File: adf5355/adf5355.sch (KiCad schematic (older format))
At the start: 96 parts, among them J1 REF_IN_A, J2 RF_B, J3 RF_A_P, J4 REF_IN_B, J5 RF_A_N, J6 Conn_01x02_Male, J7 Conn_01x10_Male, U1 L7806, U2 ADM7150, U3 ADM7150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

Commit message: Layout fully routed, now needs finilizing, moving vias to make better powerplanes, route diffpairs properly etc.
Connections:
- net labels added: GNDA
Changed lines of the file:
@@
 	6150 4900 6050 4900
 Wire Wire Line
-	5550 4900 5550 4800
-Wire Wire Line
 	5650 4800 5650 4900
-Connection ~ 5650 4900
-Wire Wire Line
-	5650 4900 5550 4900
 Wire Wire Line
 	5750 4800 5750 4900
@@
 Wire Wire Line
 	1800 6650 2100 6650
-Wire Wire Line
-	1800 6750 2100 6750
 Wire Wire Line
 	1800 6950 2100 6950
@@
 Text Label 1950 6650 0    50   ~ 0
 DATA
+Text Label 1950 6850 0    50   ~ 0
+LE
 Text Label 1950 6750 0    50   ~ 0
-LE
-Text Label 1950 6850 0    50   ~ 0
 MUX
 Wire Wire Line
@@
 	0    1    1    0
 $EndComp
-$Comp
-L power:GND #PWR053
-U 1 1 5BFF4BA3
-P 7500 5050
-F 0 "#PWR053" H 7500 4800 50  0001 C CNN
-F 1 "GND" H 7505 4877 50  0000 C CNN
-F 2 "" H 7500 5050 50  0001 C CNN
-F 3 "" H 7500 5050 50  0001 C CNN
-	1    7500 5050
-	1    0    0    -1
-$EndComp
-$Comp
-L power:GND #PWR045
-U 1 1 5BFF4C62
-P 7850 4650
-F 0 "#PWR045" H 7850 4400 50  0001 C CNN
-F 1 "GND" H 7855 4477 50  0000 C CNN
-F 2 "" H 7850 4650 50  0001 C CNN
-F 3 "" H 7850 4650 50  0001 C CNN
-	1    7850 4650
-	1    0    0    -1
-$EndComp
-$Comp
-L power:GND #PWR046
-U 1 1 5BFF4D21
-P 8400 4650
-F 0 "#PWR046" H 8400 4400 50  0001 C CNN
-F 1 "GND" H 8405 4477 50  0000 C CNN
-F 2 "" H 8400 4650 50  0001 C CNN
-F 3 "" H 8400 4650 50  0001 C CNN
-	1    8400 4650
-	1    0    0    -1
-$EndComp
-$Comp
-L power:GND #PWR047
-U 1 1 5BFF4DE0
-P 8900 4650
-F 0 "#PWR047" H 8900 4400 50  0001 C CNN
-F 1 "GND" H 8905 4477 50  0000 C CNN
-F 2 "" H 8900 4650 50  0001 C CNN
-F 3 "" H 8900 4650 50  0001 C CNN
-	1    8900 4650
-	1    0    0    -1
-$EndComp
 Wire Wire Line
 	7050 4300 7050 4050
@@
 	2500 7550 2500 7600
 Wire Wire Line
-	1800 6850 2500 6850
-Wire Wire Line
 	6950 3600 8300 3600
 Wire Wire Line
@@
 Wire Wire Line
 	2600 3450 2850 3450
+Wire Wire Line
+	2500 6850 2500 6750
+Wire Wire Line
+	1800 6750 2500 6750
+Wire Wire Line
+	1800 6850 2100 6850
+$Comp
+L power:GNDA #PWR?
+U 1 1 5C191443
+P 5550 5000
+F 0 "#PWR?" H 5550 4750 50  0001 C CNN
+F 1 "GNDA" H 5555 4827 50  0000 C CNN
+F 2 "" H 5550 5000 50  0001 C CNN
+F 3 "" H 5550 5000 50  0001 C CNN
+	1    5550 5000
+	1    0    0    -1
+$EndComp
+Wire Wire Line
+	5550 4800 5550 5000
+$Comp
+L power:GNDA #PWR?
+U 1 1 5C1A492E
+P 7500 5050
+F 0 "#PWR?" H 7500 4800 50  0001 C CNN
+F 1 "GNDA" H 7505 4877 50  0000 C CNN
+F 2 "" H 7500 5050 50  0001 C CNN
+F 3 "" H 7500 5050 50  0001 C CNN
+	1    7500 5050
+	1    0    0    -1
+$EndComp
+$Comp
+L power:GNDA #PWR?
+U 1 1 5C1A49F9
+P 7850 4650
+F 0 "#PWR?" H 7850 4400 50  0001 C CNN
+F 1 "GNDA" H 7855 4477 50  0000 C CNN
+F 2 "" H 7850 4650 50  0001 C CNN
+F 3 "" H 7850 4650 50  0001 C CNN
+	1    7850 4650
+	1    0    0    -1
+$EndComp
+$Comp
+L power:GNDA #PWR?
+U 1 1 5C1A4AC4
+P 8400 4650
+F 0 "#PWR?" H 8400 4400 50  0001 C CNN
+F 1 "GNDA" H 8405 4477 50  0000 C CNN
+F 2 "" H 8400 4650 50  0001 C CNN
+F 3 "" H 8400 4650 50  0001 C CNN
+	1    8400 4650
+	1    0    0    -1
+$EndComp
+$Comp
+L power:GNDA #PWR?
+U 1 1 5C1A4B8F
+P 8900 4650
+F 0 "#PWR?" H 8900 4400 50  0001 C CNN
+F 1 "GNDA" H 8905 4477 50  0000 C CNN
+F 2 "" H 8900 4650 50  0001 C CNN
+F 3 "" H 8900 4650 50  0001 C CNN
+	1    8900 4650
+	1    0    0    -1
+$EndComp
 $EndSCHEMATC

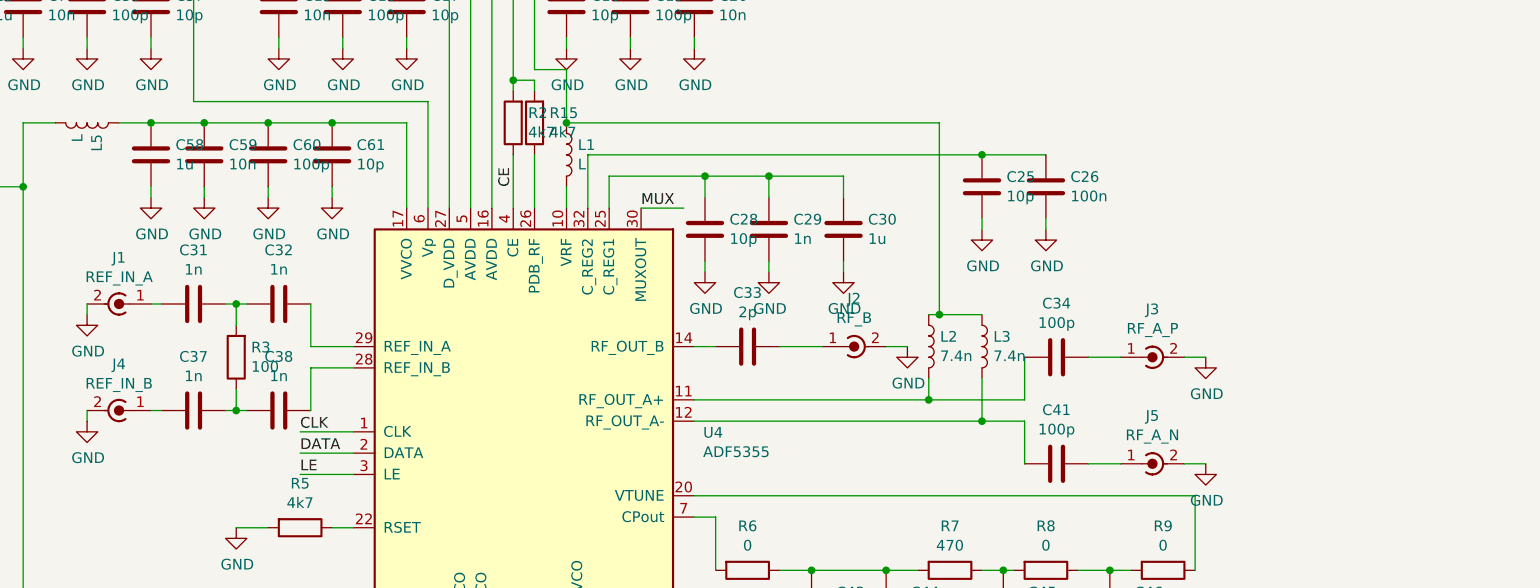
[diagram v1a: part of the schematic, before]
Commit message: Added some capacitors, better power planes etc. Needs fixing transmission lines and checking component placement for solderability. Also the c_reg capacitors probably needs to be closer to the pin
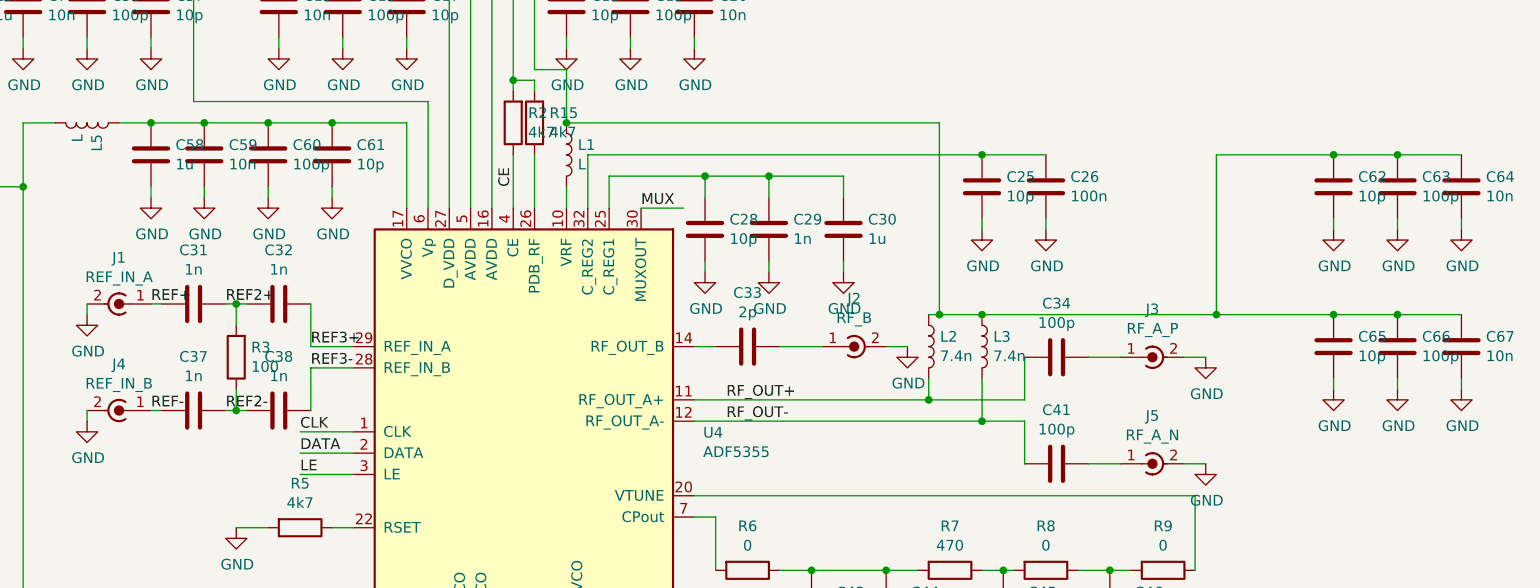
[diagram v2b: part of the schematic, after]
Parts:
- added C62, C65: 10p, Capacitors_SMD:C_0603, symbol Device:C
- added C63, C66: 100p, Capacitors_SMD:C_0603, symbol Device:C
- added C64, C67: 10n, Capacitors_SMD:C_0603, symbol Device:C
- C37: footprint Capacitors_SMD:C_0805 -> Capacitors_SMD:C_0603
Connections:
- net labels added: REF+, REF-, REF2+, REF2-, REF3+, REF3-, RF_OUT+, RF_OUT-
- wire segments 269 -> 283
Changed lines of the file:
@@
 F 0 "C37" V 4348 3550 50  0000 C CNN
 F 1 "1n" V 4439 3550 50  0000 C CNN
-F 2 "Capacitors_SMD:C_0805" H 4638 3400 50  0001 C CNN
+F 2 "Capacitors_SMD:C_0603" H 4638 3400 50  0001 C CNN
 F 3 "~" H 4600 3550 50  0001 C CNN
 	1    4600 3550
@@
 Connection ~ 3150 3250
 Wire Wire Line
-	6200 1500 6350 1500
-Wire Wire Line
 	6000 2600 6000 900
 Wire Wire Line
@@
 	1    0    0    -1
 $EndComp
-Connection ~ 6350 1500
-Wire Wire Line
-	6350 1500 6650 1500
 $Comp
 L Device:C C19
@@
 	1    0    0    -1
 $EndComp
-Connection ~ 6650 1500
-Wire Wire Line
-	6650 1500 6950 1500
 $Comp
 L Device:C C20
@@
 $EndComp
 Wire Wire Line
-	6950 1500 7300 1500
-Wire Wire Line
 	7300 1500 7300 1400
-Connection ~ 6950 1500
 Wire Wire Line
 	7300 1400 7300 900
@@
 Wire Wire Line
 	8300 3600 8500 3600
-Connection ~ 6350 2200
 $Comp
 L Device:R R15
@@
 	1800 6850 2100 6850
 $Comp
-L power:GNDA #PWR?
+L power:GNDA #PWR0109
 U 1 1 5C191443
 P 5550 5000
-F 0 "#PWR?" H 5550 4750 50  0001 C CNN
+F 0 "#PWR0109" H 5550 4750 50  0001 C CNN
 F 1 "GNDA" H 5555 4827 50  0000 C CNN
 F 2 "" H 5550 5000 50  0001 C CNN
@@
 	5550 4800 5550 5000
 $Comp
-L power:GNDA #PWR?
+L power:GNDA #PWR0110
 U 1 1 5C1A492E
 P 7500 5050
-F 0 "#PWR?" H 7500 4800 50  0001 C CNN
+F 0 "#PWR0110" H 7500 4800 50  0001 C CNN
 F 1 "GNDA" H 7505 4877 50  0000 C CNN
 F 2 "" H 7500 5050 50  0001 C CNN
@@
 $EndComp
 $Comp
-L power:GNDA #PWR?
+L power:GNDA #PWR0111
 U 1 1 5C1A49F9
 P 7850 4650
-F 0 "#PWR?" H 7850 4400 50  0001 C CNN
+F 0 "#PWR0111" H 7850 4400 50  0001 C CNN
 F 1 "GNDA" H 7855 4477 50  0000 C CNN
 F 2 "" H 7850 4650 50  0001 C CNN
@@
 $EndComp
 $Comp
-L power:GNDA #PWR?
+L power:GNDA #PWR0112
 U 1 1 5C1A4AC4
 P 8400 4650
-F 0 "#PWR?" H 8400 4400 50  0001 C CNN
+F 0 "#PWR0112" H 8400 4400 50  0001 C CNN
 F 1 "GNDA" H 8405 4477 50  0000 C CNN
 F 2 "" H 8400 4650 50  0001 C CNN
@@
 $EndComp
 $Comp
-L power:GNDA #PWR?
+L power:GNDA #PWR0113
 U 1 1 5C1A4B8F
 P 8900 4650
-F 0 "#PWR?" H 8900 4400 50  0001 C CNN
+F 0 "#PWR0113" H 8900 4400 50  0001 C CNN
 F 1 "GNDA" H 8905 4477 50  0000 C CNN
 F 2 "" H 8900 4650 50  0001 C CNN
@@
 	1    0    0    -1
 $EndComp
+Text Label 7100 3500 0    50   ~ 0
+RF_OUT+
+Text Label 7100 3600 0    50   ~ 0
+RF_OUT-
+Text Label 4400 3050 0    50   ~ 0
+REF+
+Text Label 4400 3550 0    50   ~ 0
+REF-
+Text Label 4750 3050 0    50   ~ 0
+REF2+
+Text Label 4750 3550 0    50   ~ 0
+REF2-
+Text Label 5150 3250 0    50   ~ 0
+REF3+
+Text Label 5150 3350 0    50   ~ 0
+REF3-
+Connection ~ 6350 2200
+Connection ~ 6950 1500
+Wire Wire Line
+	6950 1500 7300 1500
+Wire Wire Line
+	6650 1500 6950 1500
+Connection ~ 6650 1500
+Connection ~ 6350 1500
+Wire Wire Line
+	6350 1500 6650 1500
+Wire Wire Line
+	6200 1500 6350 1500
+$Comp
+L Device:C C62
+U 1 1 5C21E305
+P 9950 2500
+F 0 "C62" H 10065 2546 50  0000 L CNN
+F 1 "10p" H 10065 2455 50  0000 L CNN
+F 2 "Capacitors_SMD:C_0603" H 9988 2350 50  0001 C CNN
+F 3 "~" H 9950 2500 50  0001 C CNN
+	1    9950 2500
+	1    0    0    -1
+$EndComp
+$Comp
+L Device:C C63
+U 1 1 5C21E30B
+P 10250 2500
+F 0 "C63" H 10365 2546 50  0000 L CNN
+F 1 "100p" H 10365 2455 50  0000 L CNN
+F 2 "Capacitors_SMD:C_0603" H 10288 2350 50  0001 C CNN
+F 3 "~" H 10250 2500 50  0001 C CNN
+	1    10250 2500
+	1    0    0    -1
+$EndComp
+$Comp
+L Device:C C64
+U 1 1 5C21E311
+P 10550 2500
+F 0 "C64" H 10665 2546 50  0000 L CNN
+F 1 "10n" H 10665 2455 50  0000 L CNN
+F 2 "Capacitors_SMD:C_0603" H 10588 2350 50  0001 C CNN
+F 3 "~" H 10550 2500 50  0001 C CNN
+	1    10550 2500
+	1    0    0    -1
+$EndComp
+$Comp
+L power:GND #PWR0114
+U 1 1 5C21E317
+P 9950 2700
+F 0 "#PWR0114" H 9950 2450 50  0001 C CNN
+F 1 "GND" H 9955 2527 50  0000 C CNN
+F 2 "" H 9950 2700 50  0001 C CNN
+F 3 "" H 9950 2700 50  0001 C CNN
+	1    9950 2700
+	1    0    0    -1
+$EndComp
+$Comp
+L power:GND #PWR0115
+U 1 1 5C21E31D
+P 10250 2700
+F 0 "#PWR0115" H 10250 2450 50  0001 C CNN
+F 1 "GND" H 10255 2527 50  0000 C CNN
+F 2 "" H 10250 2700 50  0001 C CNN
+F 3 "" H 10250 2700 50  0001 C CNN
+	1    10250 2700
+	1    0    0    -1
+$EndComp
+$Comp
+L power:GND #PWR0116
+U 1 1 5C21E323
+P 10550 2700
+F 0 "#PWR0116" H 10550 2450 50  0001 C CNN
+F 1 "GND" H 10555 2527 50  0000 C CNN
+F 2 "" H 10550 2700 50  0001 C CNN
+F 3 "" H 10550 2700 50  0001 C CNN
+	1    10550 2700
+	1    0    0    -1
+$EndComp
+Wire Wire Line
+	9950 2650 9950 2700
+Wire Wire Line
+	10250 2650 10250 2700
+Wire Wire Line
+	10550 2650 10550 2700
+$Comp
+L Device:C C65
+U 1 1 5C245437
+P 9950 3250
+F 0 "C65" H 10065 3296 50  0000 L CNN
+F 1 "10p" H 10065 3205 50  0000 L CNN
+F 2 "Capacitors_SMD:C_0603" H 9988 3100 50  0001 C CNN
+F 3 "~" H 9950 3250 50  0001 C CNN
+	1    9950 3250
+	1    0    0    -1
+$EndComp
+$Comp
+L Device:C C66
+U 1 1 5C24543D
+P 10250 3250
+F 0 "C66" H 10365 3296 50  0000 L CNN
+F 1 "100p" H 10365 3205 50  0000 L CNN
+F 2 "Capacitors_SMD:C_0603" H 10288 3100 50  0001 C CNN
+F 3 "~" H 10250 3250 50  0001 C CNN
+	1    10250 3250
+	1    0    0    -1
+$EndComp
+$Comp
+L Device:C C67
+U 1 1 5C245443
+P 10550 3250
+F 0 "C67" H 10665 3296 50  0000 L CNN
+F 1 "10n" H 10665 3205 50  0000 L CNN
+F 2 "Capacitors_SMD:C_0603" H 10588 3100 50  0001 C CNN
+F 3 "~" H 10550 3250 50  0001 C CNN
+	1    10550 3250
+	1    0    0    -1
+$EndComp
+$Comp
+L power:GND #PWR0117
+U 1 1 5C245449
+P 9950 3450
+F 0 "#PWR0117" H 9950 3200 50  0001 C CNN
+F 1 "GND" H 9955 3277 50  0000 C CNN
+F 2 "" H 9950 3450 50  0001 C CNN
+F 3 "" H 9950 3450 50  0001 C CNN
+	1    9950 3450
+	1    0    0    -1
+$EndComp
+$Comp
+L power:GND #PWR0118
+U 1 1 5C24544F
+P 10250 3450
+F 0 "#PWR0118" H 10250 3200 50  0001 C CNN
+F 1 "GND" H 10255 3277 50  0000 C CNN
+F 2 "" H 10250 3450 50  0001 C CNN
+F 3 "" H 10250 3450 50  0001 C CNN
+	1    10250 3450
+	1    0    0    -1
+$EndComp
+$Comp
+L power:GND #PWR0119
+U 1 1 5C245455
+P 10550 3450
+F 0 "#PWR0119" H 10550 3200 50  0001 C CNN
+F 1 "GND" H 10555 3277 50  0000 C CNN
+F 2 "" H 10550 3450 50  0001 C CNN
+F 3 "" H 10550 3450 50  0001 C CNN
+	1    10550 3450
+	1    0    0    -1
+$EndComp
+Wire Wire Line
+	9950 3400 9950 3450
+Wire Wire Line
+	10250 3400 10250 3450
+Wire Wire Line
+	10550 3400 10550 3450
+Wire Wire Line
+	10550 2350 10250 2350
+Connection ~ 10250 2350
+Wire Wire Line
+	10250 2350 9950 2350
+Wire Wire Line
+	10550 3100 10250 3100
+Connection ~ 10250 3100
+Wire Wire Line
+	10250 3100 9950 3100
+Wire Wire Line
+	9950 3100 9400 3100
+Connection ~ 9950 3100
+Connection ~ 8300 3100
+Wire Wire Line
+	9950 2350 9400 2350
+Wire Wire Line
+	9400 2350 9400 3100
+Connection ~ 9950 2350
+Connection ~ 9400 3100
+Wire Wire Line
+	9400 3100 8300 3100
 $EndSCHEMATC
